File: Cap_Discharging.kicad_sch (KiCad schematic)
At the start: 5 parts, among them Q1 ZVP4424A, T51 ZTX857, U53 ILD213T

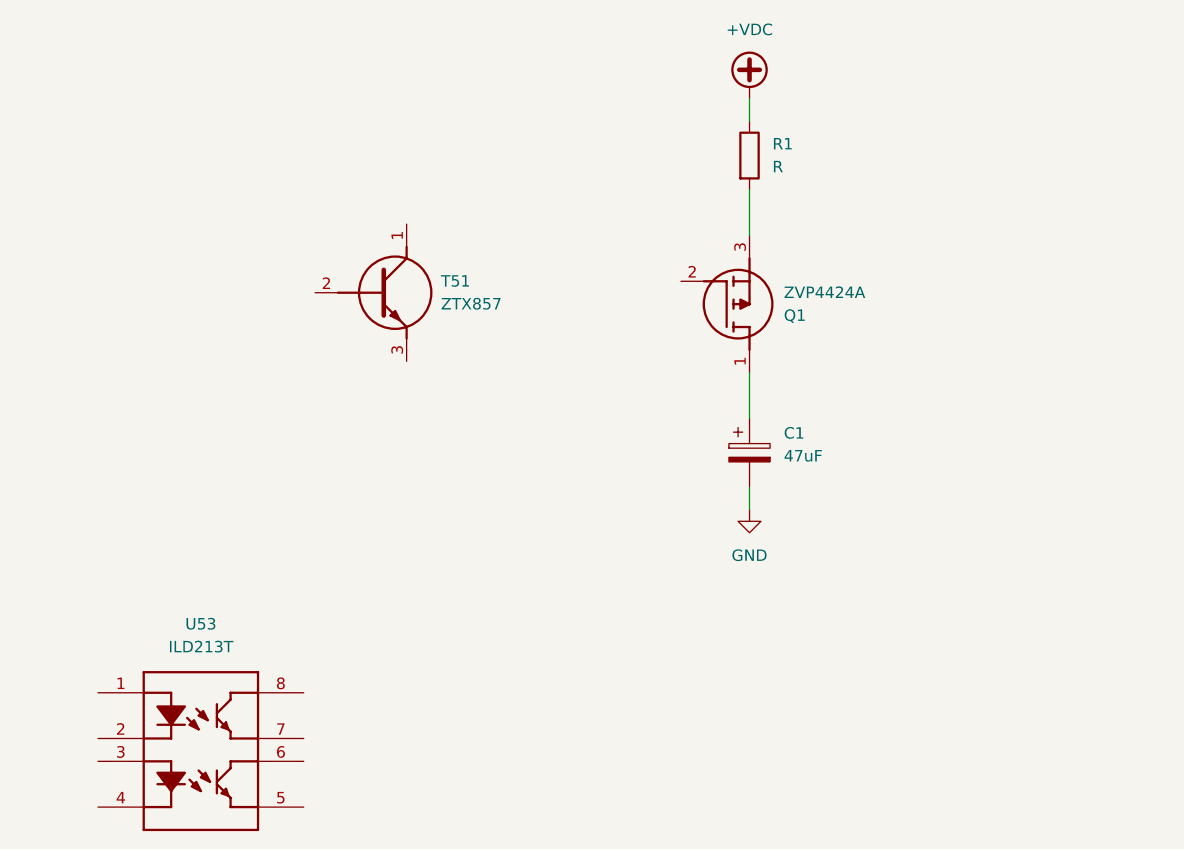
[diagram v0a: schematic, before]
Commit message: Added second cap charge
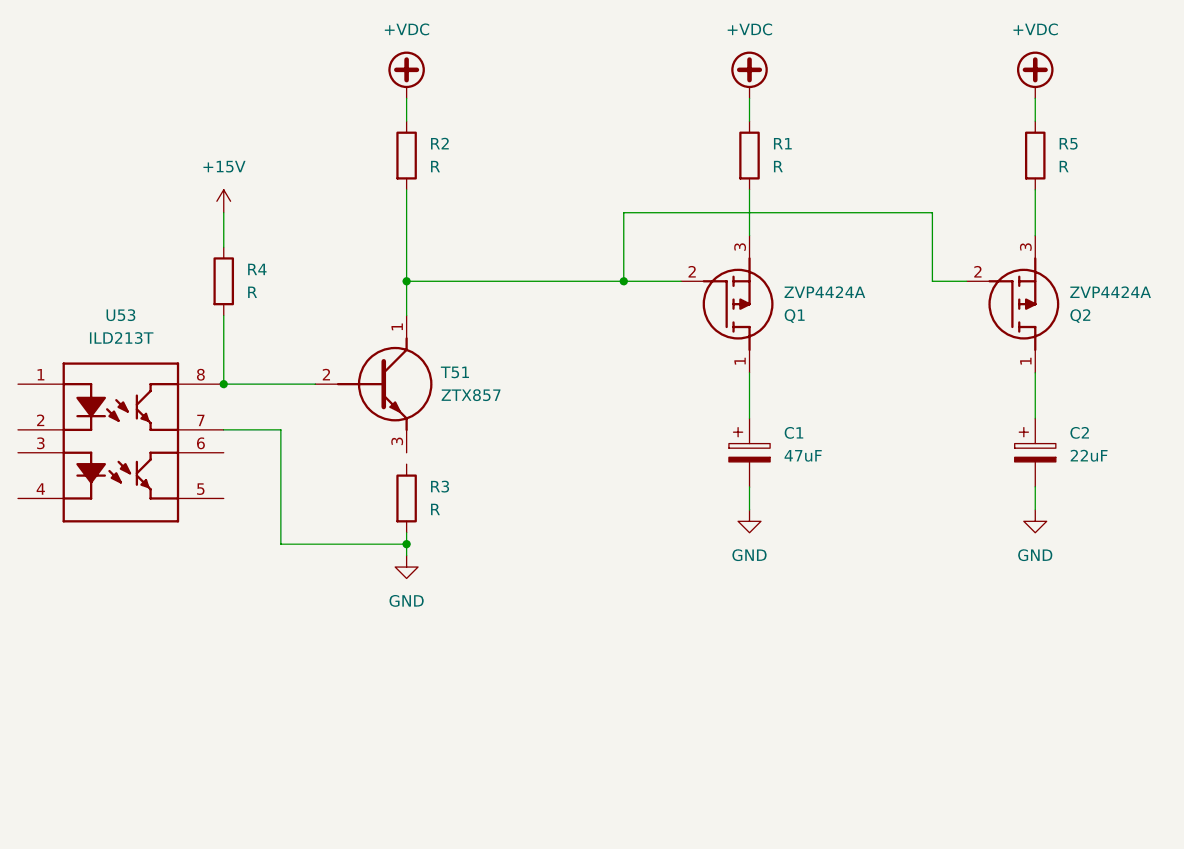
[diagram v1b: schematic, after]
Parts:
- added C2: 22uF, symbol Amada_symbols:CAP_P
- added Q2: ZVP4424A, E-LINE_BULK, symbol Amada_symbols:ZVP4424A
- added R2, R3, R4, R5: R, symbol Device:R
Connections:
- net +VDC: now also R2.1, R5.1
- net GND: now also U53.7 (EMITTER_2), C2.2, R3.2
- net at Q1.2 (G): now also T51.1 (C), Q2.2 (G), R2.2
- net at U53.8 (COLLECTOR_2): now also T51.2 (B), R4.2
- new net: Q2.3 (S), R5.2
- new net: C2.1, Q2.1 (D)
- new net +15V: R4.1
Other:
- moved on the sheet: T51, U53
